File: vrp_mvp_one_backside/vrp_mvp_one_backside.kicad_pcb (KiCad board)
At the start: 2 copper layers, 77 x 150 mm, 24 parts, among them J2 BACKSIDE_INTERFACE, J3 Bus_PCI_Express_Mini, J4 SIM TRAY, J7 BACKSIDE_INTERFACE_2, Q1 DMN3042L, Q2 MMBT2222A, U1 MAX712CSE, U3 AZ1084-3.3, U4 MIC5501-3.0YM5

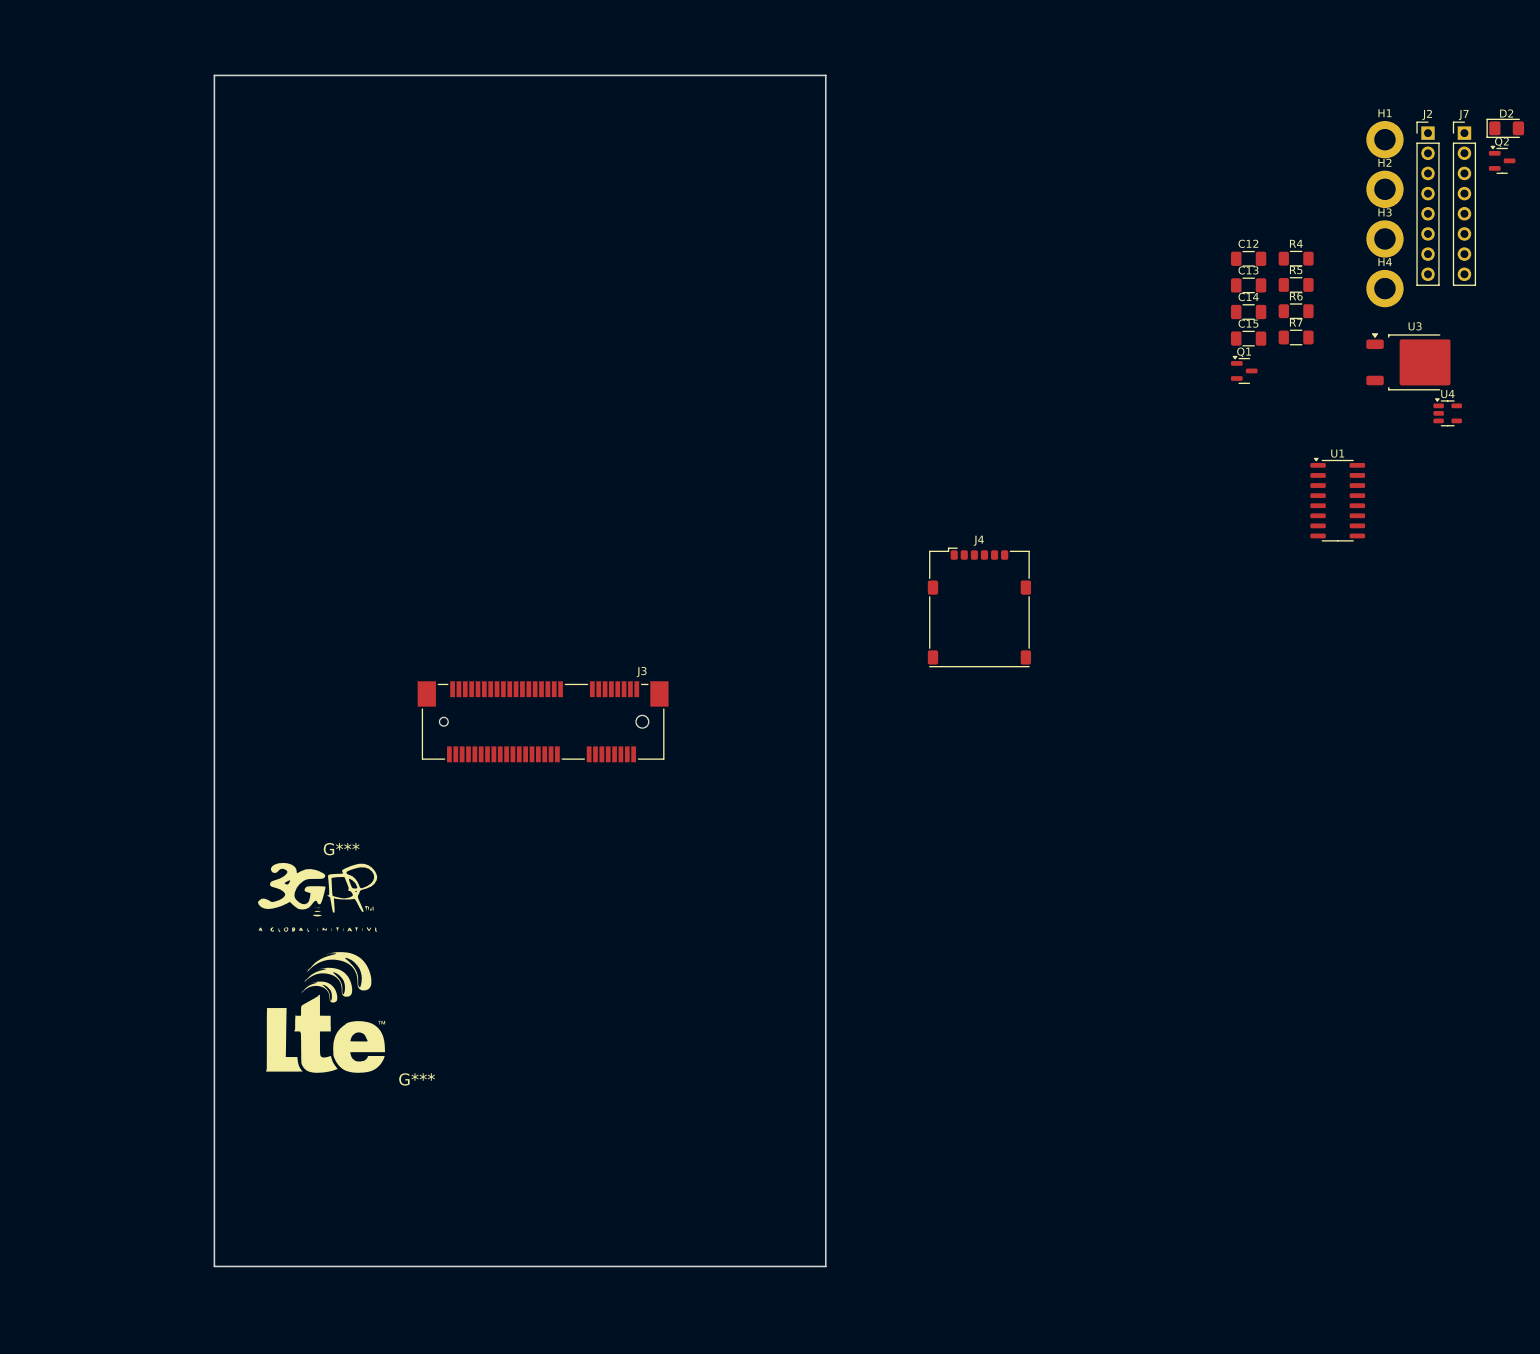
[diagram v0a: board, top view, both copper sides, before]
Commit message: audio, more routing, switched to lipo battery
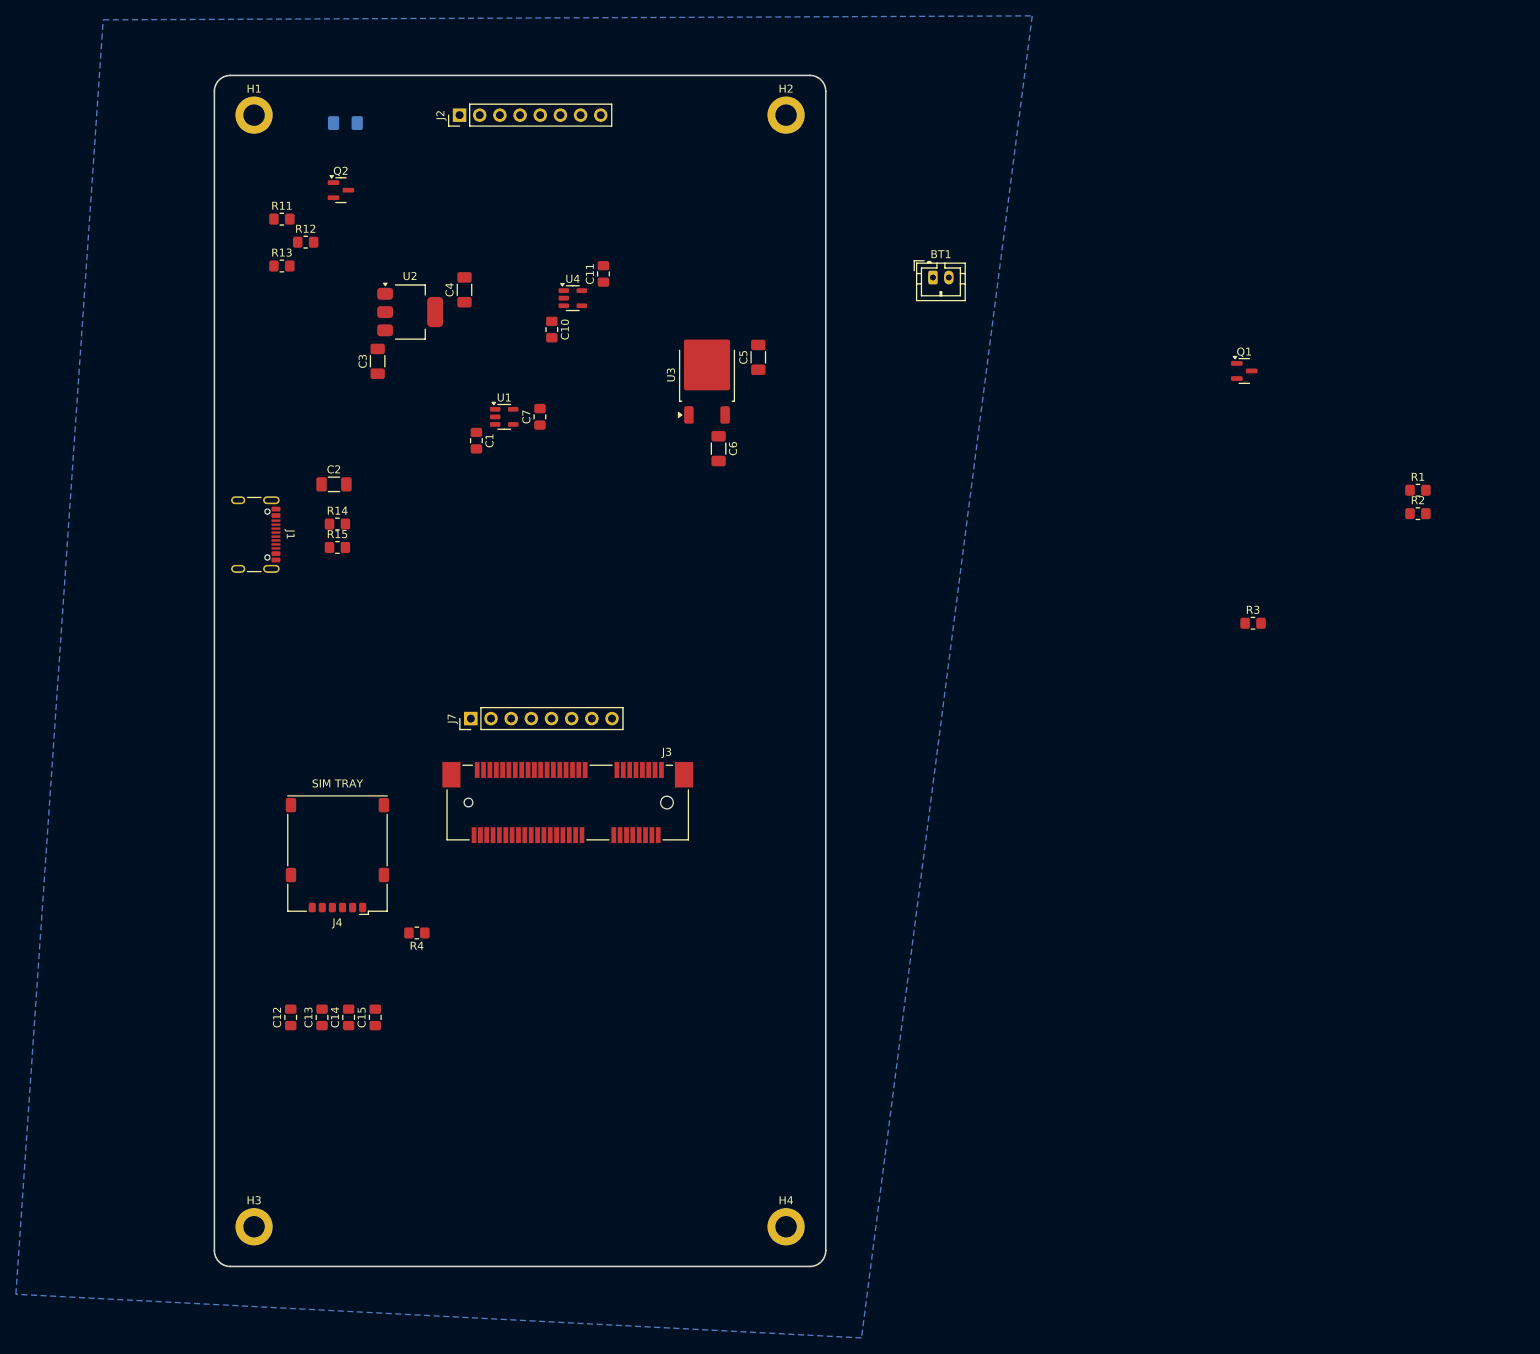
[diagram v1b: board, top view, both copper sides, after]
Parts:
- removed R5, R6, R7: 0, Resistor_SMD:R_1206_3216Metric_Pad1.30x1.75mm_HandSolder
- added BT1: LIPO, Connector_JST:JST_PH_B2B-PH-K_1x02_P2.00mm_Vertical, F.Cu at (179.0, 52.0)
- added C1: 4.7uF, Capacitor_SMD:C_0805_2012Metric_Pad1.18x1.45mm_HandSolder, F.Cu at (121.5, 72.5)
- added C10: 1uF, Capacitor_SMD:C_0805_2012Metric_Pad1.18x1.45mm_HandSolder, F.Cu at (131.0, 58.5)
- added C11: 1uF, Capacitor_SMD:C_0805_2012Metric_Pad1.18x1.45mm_HandSolder, F.Cu at (137.5, 51.5)
- added C2: 10uF, Capacitor_SMD:C_1206_3216Metric_Pad1.33x1.80mm_HandSolder, F.Cu at (103.6, 78.0)
- added C3: 10uF, Capacitor_SMD:C_1206_3216Metric_Pad1.33x1.80mm_HandSolder, F.Cu at (109.1, 62.5)
- added C4: 22uF, Capacitor_SMD:C_1206_3216Metric_Pad1.33x1.80mm_HandSolder, F.Cu at (120.0, 53.5)
- added C5: 22uF, Capacitor_SMD:C_1206_3216Metric_Pad1.33x1.80mm_HandSolder, F.Cu at (157.0, 62.0)
- added C6: 10uF, Capacitor_SMD:C_1206_3216Metric_Pad1.33x1.80mm_HandSolder, F.Cu at (152.0, 73.5)
- added C7: 4.7uF, Capacitor_SMD:C_0805_2012Metric_Pad1.18x1.45mm_HandSolder, F.Cu at (129.5, 69.5)
- added J1: USB_C_Receptacle_USB2.0_16P, Connector_USB:USB_C_Receptacle_GCT_USB4105-xx-A_16P_TopMnt_Horizontal, F.Cu at (92.6, 84.3)
- added R1: 10k, Resistor_SMD:R_0805_2012Metric_Pad1.20x1.40mm_HandSolder, F.Cu at (240.1, 78.7)
- added R11: R_US, Resistor_SMD:R_0805_2012Metric_Pad1.20x1.40mm_HandSolder, F.Cu at (97.0, 44.6)
- added R12: 10k, Resistor_SMD:R_0805_2012Metric_Pad1.20x1.40mm_HandSolder, F.Cu at (100.0, 47.5)
- added R13: 100, Resistor_SMD:R_0805_2012Metric_Pad1.20x1.40mm_HandSolder, F.Cu at (97.0, 50.5)
- added R14: 90, Resistor_SMD:R_0805_2012Metric_Pad1.20x1.40mm_HandSolder, F.Cu at (104.0, 83.0)
- added R15: 90, Resistor_SMD:R_0805_2012Metric_Pad1.20x1.40mm_HandSolder, F.Cu at (104.0, 86.0)
- added R2: 100, Resistor_SMD:R_0805_2012Metric_Pad1.20x1.40mm_HandSolder, F.Cu at (240.1, 81.7)
- added R3: 2k, Resistor_SMD:R_0805_2012Metric_Pad1.20x1.40mm_HandSolder, F.Cu at (219.3, 95.5)
- added U2: AZ1117-1.8, Package_TO_SOT_SMD:SOT-223-3_TabPin2, F.Cu at (113.2, 56.3)
- C12, C13, C14, C15: footprint Capacitor_SMD:C_1206_3216Metric_Pad1.33x1.80mm_HandSolder -> Capacitor_SMD:C_0805_2012Metric_Pad1.18x1.45mm_HandSolder
- D2, G*** (x2): moved to B.Cu
- R4: footprint Resistor_SMD:R_1206_3216Metric_Pad1.30x1.75mm_HandSolder -> Resistor_SMD:R_0805_2012Metric_Pad1.20x1.40mm_HandSolder
- U1: value MAX712CSE -> MCP73831-3-OT; footprint Package_SO:SOIC-16_3.9x9.9mm_P1.27mm -> Package_TO_SOT_SMD:SOT-23-5
- moved H3 189.1 mm to (93.5, 171.5)
- moved C12 153.9 mm to (98.1, 145.1), turned to 90 degrees
- moved C13 148.7 mm to (102.1, 145.1), turned to 90 degrees
- moved Q2 146.3 mm to (104.4, 41.0)
- moved D2 146.3 mm to (105.0, 32.5)
- moved J7 145.2 mm to (120.8, 107.5), turned to 90 degrees
- moved C14 144.0 mm to (105.4, 145.1), turned to 90 degrees
- moved H1 142.5 mm to (93.5, 31.5)
- moved H4 140.2 mm to (160.5, 171.5)
- moved R4 139.6 mm to (114.0, 134.5), turned to 180 degrees
- moved C15 139.3 mm to (108.8, 145.1), turned to 90 degrees
- moved J2 122.0 mm to (119.4, 31.5), turned to 90 degrees
- moved U4 111.1 mm to (133.6, 54.5)
- moved U1 105.5 mm to (125.0, 69.5)
- moved U3 89.2 mm to (150.5, 64.2), turned to 90 degrees
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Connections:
- C12 pad 1: Net-(J4-I/O) -> USIM_DATA
- C12 pad 2: GND -> VBAT-
- C13 pad 1: Net-(J4-CLK) -> USIM_CLK
- C13 pad 2: GND -> VBAT-
- C14 pad 1: Net-(J4-RST) -> USIM_RST
- C14 pad 2: GND -> VBAT-
- C15 pad 2: GND -> VBAT-
- H1 pad 1: GND -> VBAT-
- H2 pad 1: GND -> VBAT-
- H3 pad 1: GND -> VBAT-
- H4 pad 1: GND -> VBAT-
- J2 pad 1: GND -> VBAT-
- J2 pad 8: GND -> VBAT-
- J3 pad 36: MODEM_USB_D_ -> Net-(J3-USB_D-)
- J3 pad 38: MODEM_USB_D+ -> Net-(J3-USB_D+)
- J3 pad 45: PCM_CLK -> PCM_MODEM_CLK
- J3 pad 47: PCM_CODEC_DIN -> PCM_MODEM_DOUT
- J3 pad 49: PCM_CODEC_DOUT -> PCM_MODEM_DIN
- J3 pad 51: PCM_SYNC -> PCM_MODEM_SYNC
- J4 pad 2: Net-(J4-RST) -> USIM_RST
- J4 pad 3: Net-(J4-CLK) -> USIM_CLK
- J4 pad 5: GND -> VBAT-
- J4 pad 7: Net-(J4-I/O) -> USIM_DATA
- J7 pad 1: GND -> VBAT-
- J7 pad 2: LED_FLASH_ENABLE -> PCM_MODEM_CLK
- J7 pad 3: unconnected-(J7-Pin_3-Pad3) -> PCM_MODEM_SYNC
- J7 pad 4: unconnected-(J7-Pin_4-Pad4) -> PCM_MODEM_DIN
- J7 pad 5: unconnected-(J7-Pin_5-Pad5) -> PCM_MODEM_DOUT
- J7 pad 7: unconnected-(J7-Pin_7-Pad7) -> LED_FLASH_ENABLE
- J7 pad 8: GND -> VBAT-
- Q1 pad 2: GND -> VBAT-
- Q2 pad 2: GND -> VBAT-
- R4 pad 2: Net-(J4-I/O) -> USIM_DATA
- U1 pad 1: Net-(U1-REF) -> CHARGE_STATUS
- U1 pad 2: VBAT+ -> VBAT-
- U1 pad 3: unconnected-(U1-PGM0-Pad3) -> VBAT+
- U1 pad 4: unconnected-(U1-PGM1-Pad4) -> VBUS
- U1 pad 5: Net-(U1-THI) -> Net-(U1-PROG)
- U3 pad 1: GND -> VBAT-
- U3 pad 3: VCC -> VBAT+
- U4 pad 1: VCC -> VBAT+
- U4 pad 2: GND -> VBAT-
- U4 pad 3: VCC -> VBAT+
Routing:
- added copper zone on B.Cu, net GND
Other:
- outline, holes or cut-outs redrawn
- board text added: "LED FLASH"
- board text added: "MODEM/POWER"
- board text added: "REV 0"
- board text added: "SPANAWAY BACKSIDE"
- board text added: "VoLTE RETROFIT PROJECT"

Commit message: forgot to save
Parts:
- moved J7 66.0 mm to (118.4, 173.5)
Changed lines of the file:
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@@
 	(footprint "Connector_PinHeader_2.54mm:PinHeader_1x08_P2.54mm_Vertical"
 		(layer "F.Cu")
-		(at 120.8 107.5 90)
+		(at 118.38 173.5 90)
 		(descr "Through hole straight pin header, 1x08, 2.54mm pitch, single row")
 		(tags "Through hole pin header THT 1x08 2.54mm single row")

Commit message: more routing and part placement
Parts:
- added D1: SP0504BAHT, Package_TO_SOT_SMD:SOT-23-5, F.Cu at (104.5, 111.6)
- moved R2 129.7 mm to (114.0, 112.0)
- moved R1 126.9 mm to (117.5, 111.4), turned to 90 degrees
- moved Q1 114.4 mm to (116.5, 115.9), turned to -90 degrees
- moved R3 97.2 mm to (127.0, 65.0), turned to 90 degrees
- moved BT1 20.2 mm to (159.0, 49.5)
- moved R4 12.9 mm to (103.5, 142.0)
- moved C12 11.6 mm to (98.5, 133.5), turned to 180 degrees
- moved C15 10.6 mm to (108.5, 134.5), turned to -90 degrees
- moved C13 9.59 mm to (102.0, 135.5), turned to -90 degrees
- moved C14 8.14 mm to (105.0, 137.0), turned to -90 degrees
- moved J3 4.50 mm to (137.5, 117.9)
- moved J7 2.02 mm to (118.1, 171.5)
- moved C3 1.46 mm to (108.0, 61.5), turned to 180 degrees
- moved J2 1.27 mm to (118.1, 31.5)
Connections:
- J2 pad 4: 5V -> VBAT+
- J2 pad 5: MODEM_UART_TX -> UART_MODEM_TX
- J2 pad 6: MODEM_UART_RX -> UART_MODEM_RX
- J7 pad 6: unconnected-(J7-Pin_6-Pad6) -> CHARGE_STATUS
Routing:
- net PCM_MODEM_SYNC: track 0.00 -> 105.2 mm
- net PCM_MODEM_DIN: track 0.00 -> 104.4 mm
- net PCM_MODEM_DOUT: track 0.00 -> 104.0 mm
- net PCM_MODEM_CLK: track 0.00 -> 103.4 mm
- net USIM_DATA: track 0.00 -> 87.5 mm, vias 0 -> 2
- net USIM_VDD: track 0.00 -> 85.8 mm
- net USIM_CLK: track 0.00 -> 71.9 mm, vias 0 -> 2
- net USIM_RST: track 0.00 -> 69.8 mm, vias 0 -> 2
- net MODEM_SINK: track 0.00 -> 45.1 mm, vias 0 -> 11
- net UART_MODEM_TX: track 0.00 -> 23.0 mm
- net UART_MODEM_RX: track 0.00 -> 22.9 mm
- net VBAT-: track 0.00 -> 7.57 mm, vias 0 -> 5
- added copper zone on F.Cu, net MODEM_SINK
- added copper zone on B.Cu, net VBAT-
- removed copper zone on B.Cu, net GND
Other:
- board text added: "3.3V"
- board text added: "3V"
- board text added: "CHRG"
- board text added: "CLK"
- board text added: "DIN"
- board text added: "DOUT"
- board text added: "FLSH"
- board text added: "GND"
- board text added: "MODEM_EN"
- board text added: "RX"
- board text added: "SYNC"
- board text added: "TX"
- board text added: "VBAT"

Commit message: changes
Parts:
- removed C3: 10uF, Capacitor_SMD:C_1206_3216Metric_Pad1.33x1.80mm_HandSolder
- removed C4: 22uF, Capacitor_SMD:C_1206_3216Metric_Pad1.33x1.80mm_HandSolder
- removed Q1: DMN3042L, Package_TO_SOT_SMD:SOT-23
- removed R1: 10k, Resistor_SMD:R_0805_2012Metric_Pad1.20x1.40mm_HandSolder
- removed R2: 100, Resistor_SMD:R_0805_2012Metric_Pad1.20x1.40mm_HandSolder
- removed U2: AZ1117-1.8, Package_TO_SOT_SMD:SOT-223-3_TabPin2
- moved BT1 61.3 mm to (98.0, 55.5), turned to 90 degrees
- moved U3 43.6 mm to (110.5, 46.9)
- moved C5 42.6 mm to (117.5, 46.0), turned to 0 degrees
- moved C6 41.4 mm to (115.0, 55.0), turned to 0 degrees
- moved C1 24.3 mm to (97.5, 69.0)
- moved C7 24.2 mm to (105.5, 66.5)
- moved R3 24.1 mm to (103.0, 63.0)
- moved U1 23.5 mm to (101.6, 67.0)
- moved C10 16.3 mm to (115.0, 61.5)
- moved C11 15.2 mm to (124.5, 59.5), turned to 0 degrees
- moved U4 15.0 mm to (119.9, 60.5)
- moved R11 9.92 mm to (99.5, 35.0), turned to -90 degrees
- moved R13 7.16 mm to (100.0, 44.0), turned to -90 degrees
- moved Q2 5.03 mm to (99.5, 40.0), turned to 90 degrees
- moved R12 4.03 mm to (98.0, 44.0), turned to 90 degrees
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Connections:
- J1 pad B7: MODEM_USB_D+ -> MODEM_USB_D-
- J2 pad 5: UART_MODEM_TX -> UART_MODEM_RX
- J2 pad 6: UART_MODEM_RX -> UART_MODEM_TX
- J3 pad 15: MODEM_SINK -> VBAT-
- J3 pad 18: MODEM_SINK -> VBAT-
- J3 pad 21: MODEM_SINK -> VBAT-
- J3 pad 26: MODEM_SINK -> VBAT-
- J3 pad 27: MODEM_SINK -> VBAT-
- J3 pad 29: MODEM_SINK -> VBAT-
- J3 pad 34: MODEM_SINK -> VBAT-
- J3 pad 35: MODEM_SINK -> VBAT-
- J3 pad 37: MODEM_SINK -> VBAT-
- J3 pad 4: MODEM_SINK -> VBAT-
- J3 pad 40: MODEM_SINK -> VBAT-
- J3 pad 43: MODEM_SINK -> VBAT-
- J3 pad 50: MODEM_SINK -> VBAT-
- J3 pad 9: MODEM_SINK -> VBAT-
- J7 pad 3: PCM_MODEM_SYNC -> PCM_MODEM_DOUT
- J7 pad 5: PCM_MODEM_DOUT -> PCM_MODEM_SYNC
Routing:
- net LED_FLASH_ENABLE: track 0.00 -> 182.4 mm, vias 0 -> 2
- net CHARGE_STATUS: track 0.00 -> 181.8 mm, vias 0 -> 2
- net 3.3V: track 0.00 -> 162.2 mm, vias 0 -> 5
- net UART_MODEM_RX: track 22.9 -> 125.7 mm
- net UART_MODEM_TX: track 23.0 -> 121.6 mm
- net Net-(J3-USB_D-): track 0.00 -> 62.3 mm
- net Net-(J3-USB_D+): track 0.00 -> 60.9 mm
- net VBUS: track 0.00 -> 49.9 mm
- net VBAT+: track 0.00 -> 48.8 mm
- net VBAT-: track 7.57 -> 52.7 mm, vias 5 -> 29
- net MODEM_SINK: track 45.1 -> 0.00 mm, vias 11 -> 0
- net 3V: track 0.00 -> 30.6 mm
- net MODEM_USB_D-: track 0.00 -> 12.3 mm, vias 0 -> 2
- net MODEM_USB_D+: track 0.00 -> 11.9 mm, vias 0 -> 2
- net Net-(D2-K): track 0.00 -> 6.22 mm, vias 0 -> 1
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- removed copper zone on F.Cu, net MODEM_SINK

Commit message: very close to authoring rev 0
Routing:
- net VBAT+: track 48.8 -> 81.8 mm, vias 0 -> 2
- net VBAT-: track 52.7 -> 55.6 mm, vias 29 -> 31
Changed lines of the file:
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@@
+	)
+	(segment
+		(start 125.73 51.27)
+		(end 125.73 31.5)
+		(width 0.5)
+		(layer "F.Cu")
+		(net 53)
+	)
+	(segment
+		(start 119.475 51.975)
+		(end 119.5 52)
+		(width 0.5)
+		(layer "F.Cu")
+		(net 53)
+	)
+	(segment
+		(start 125 52)
+		(end 125.73 51.27)
+		(width 0.5)
+		(layer "F.Cu")
+		(net 53)
 	)
 	(segment
@@
 	)
 	(segment
+		(start 112.805 51.975)
+		(end 119.475 51.975)
+		(width 0.5)
+		(layer "F.Cu")
+		(net 53)
+	)
+	(segment
 		(start 97.5 67.9625)
 		(end 97.5 63.5)
@@
 		(net 53)
 	)
+	(via
+		(at 119.5 52)
+		(size 0.6)
+		(drill 0.3)
+		(layers "F.Cu" "B.Cu")
+		(net 53)
+	)
+	(via
+		(at 125 52)
+		(size 0.6)
+		(drill 0.3)
+		(layers "F.Cu" "B.Cu")
+		(net 53)
+	)
+	(segment
+		(start 119.5 52)
+		(end 125 52)
+		(width 0.5)
+		(layer "B.Cu")
+		(net 53)
+	)
 	(segment
 		(start 135.7 113.8)
@@
 	)
 	(segment
+		(start 125.575 59.45)
+		(end 126.95 59.45)
+		(width 0.2)
+		(layer "F.Cu")
+		(net 54)
+	)
+	(segment
 		(start 148.1 122)
 		(end 148.1 123.6)
@@
 	)
 	(segment
+		(start 126.95 59.45)
+		(end 127 59.5)
+		(width 0.2)
+		(layer "F.Cu")
+		(net 54)
+	)
+	(segment
 		(start 108.5 135.5375)
 		(end 108.5 137)
@@
 		(net 54)
 	)
+	(segment
+		(start 115 62.575)
+		(end 115 64)
+		(width 0.2)
+		(layer "F.Cu")
+		(net 54)
+	)
 	(via
 		(at 110 52)
@@
 	)
 	(via
+		(at 115 64)
+		(size 0.6)
+		(drill 0.3)
+		(layers "F.Cu" "B.Cu")
+		(net 54)
+	)
+	(via
 		(at 105 139.5)
 		(size 0.6)
@@
 		(size 0.6)
 		(drill 0.3)
+		(layers "F.Cu" "B.Cu")
+		(net 54)
+	)
+	(via
+		(at 127 59.5)
+		(size 0.6)
+		(drill 0.3)

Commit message: response to issue 1
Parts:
- moved G*** 6.00 mm to (139.5, 143.0)
- moved G*** 6.00 mm to (117.0, 146.0)
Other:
- board text added: "FLASH"
- board text removed: "FLSH"
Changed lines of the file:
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@@
 		(property "Value" "SIM TRAY"
 			(at 0 8.5 0)
-			(layer "F.SilkS")
+			(layer "F.SilkS" knockout)
 			(effects
 				(font
 					(size 1 1)
-					(thickness 0.15)
+					(thickness 0.2)
+					(bold yes)
 				)
 			)
@@
 		(tags "mini pcie")
 		(property "Reference" "J3"
-			(at -17 -52.1 0)
+			(at 0 6.4 0)
 			(layer "F.SilkS")
 			(effects
@@
 	(footprint "logos:lte_logo"
 		(layer "B.Cu")
-		(at 139.5 149 180)
+		(at 139.5 143 180)
 		(property "Reference" "G***"
 			(at 11.5 -8.5 0)
@@
 	(footprint "logos:3gpp_logo"
 		(layer "B.Cu")
-		(at 117 152 180)
+		(at 117 146 180)
 		(property "Reference" "G***"
 			(at 3 6 0)
@@
 	)
 	(gr_text "REV 0"
-		(at 130.657143 168 -0)
+		(at 130.657143 162 -0)
 		(layer "B.SilkS")
 		(effects
@@
 	)
 	(gr_text "VoLTE RETROFIT PROJECT"
-		(at 141.585715 162.5 0)
+		(at 141.585715 156.5 0)
 		(layer "B.SilkS")
 		(effects
@@
 	)
 	(gr_text "DOUT"
-		(at 129 173 -270)
+		(at 129 165 -270)
 		(layer "B.SilkS")
 		(effects
@@
 	)
 	(gr_text "DIN"
-		(at 126.5 173 -270)
+		(at 126.5 166 -270)
 		(layer "B.SilkS")
 		(effects
@@
 	)
 	(gr_text "GND"
-		(at 136.5 173 -270)
+		(at 136.5 166 -270)
 		(layer "B.SilkS")
 		(effects
@@
 	)
 	(gr_text "CLK"
-		(at 121.5 173 -270)
+		(at 121.5 166 -270)
 		(layer "B.SilkS")
 		(effects
@@
 	)
 	(gr_text "CHRG"
-		(at 131.5 173 -270)
+		(at 131.5 165 -270)
 		(layer "B.SilkS")
 		(effects
@@
 	)
 	(gr_text "SPANAWAY BACKSIDE"
-		(at 138.942857 165.5 -0)
+		(at 138.942857 159.5 -0)
 		(layer "B.SilkS")
 		(effects
@@
 	)
 	(gr_text "GND"
-		(at 118.5 173 -270)
+		(at 119 166 -270)
 		(layer "B.SilkS")
 		(effects
@@
 		)
 	)
-	(gr_text "FLSH"
-		(at 133.5 173 -270)
+	(gr_text "FLASH"
+		(at 134 164.5 -270)
 		(layer "B.SilkS")
 		(effects
@@
 	(gr_text "MODEM/POWER"
 		(at 98 93 270)
-		(layer "B.SilkS")
+		(layer "B.SilkS" knockout)
 		(effects
 			(font
 				(size 1.5 1.5)
-				(thickness 0.1875)
+				(thickness 0.3)
+				(bold yes)
 			)
 			(justify left bottom mirror)
@@
 	)
 	(gr_text "SYNC"
-		(at 124 173 -270)
+		(at 124 165 -270)
 		(layer "B.SilkS")
 		(effects
